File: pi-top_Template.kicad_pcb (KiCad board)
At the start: 2 copper layers, 65 x 56 mm, 6 parts, among them J1 CONN_02X17, J2 CONN_02X17

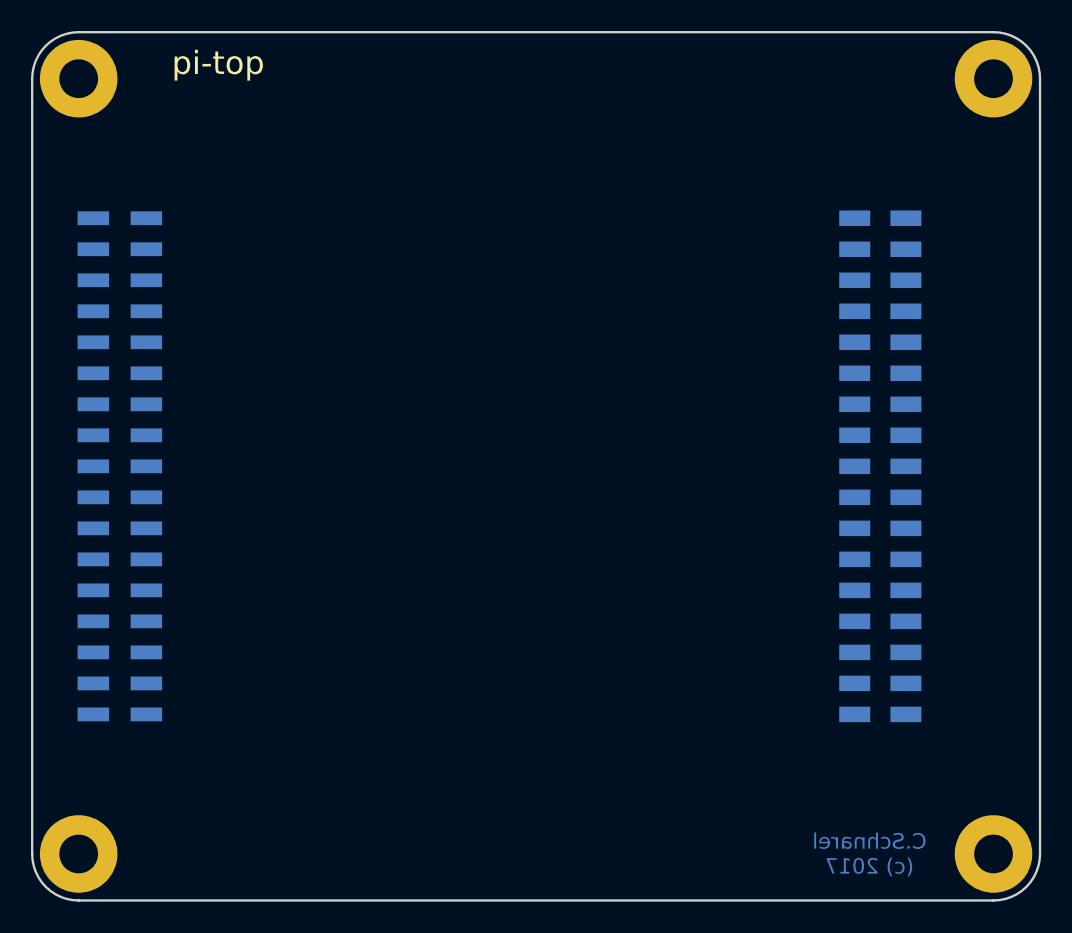
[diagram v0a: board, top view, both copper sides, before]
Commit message: Added board dimentsions
Corrected mounting hole spacing
Corrected connector labeling
Updated README with board size tips
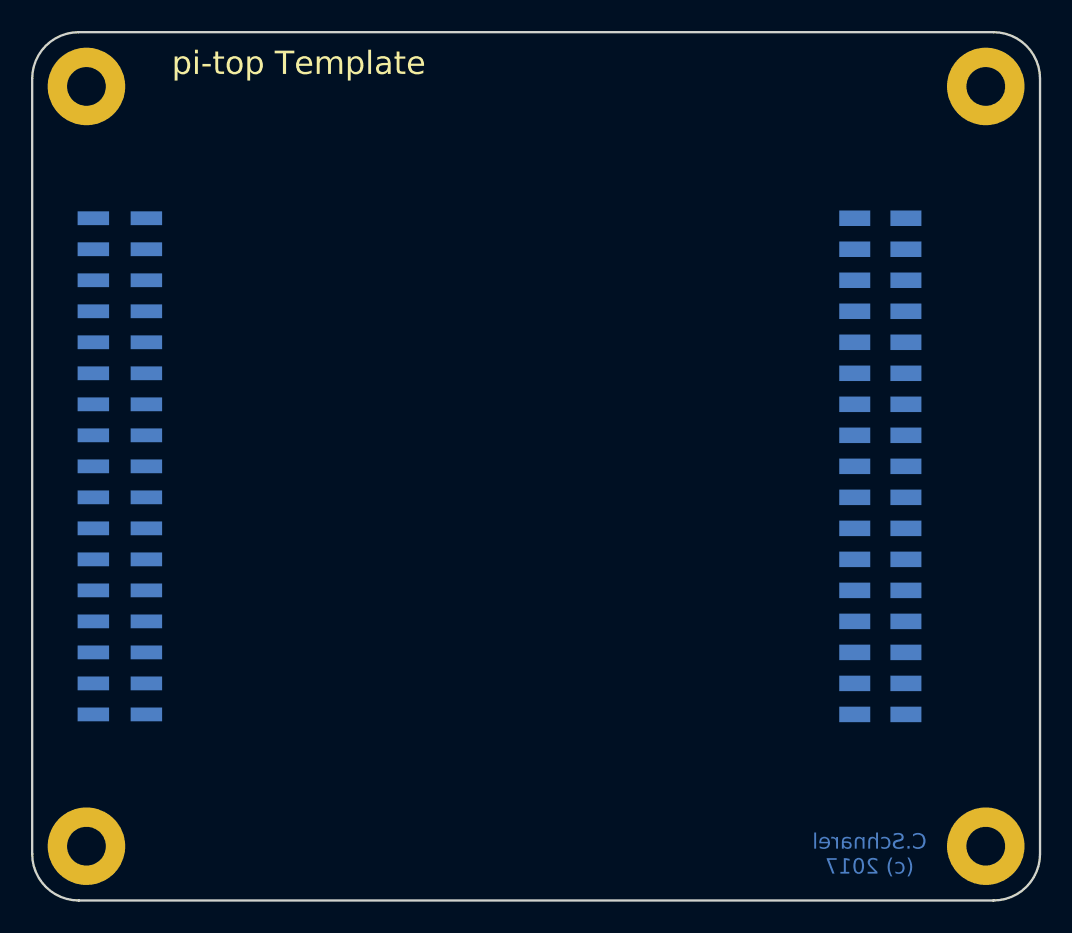
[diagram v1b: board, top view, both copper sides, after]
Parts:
- J1: value CONN_02X17 -> 3M 951 series
- J2: value CONN_02X17 -> Harwin M22-655R
- moved M** 0.71 mm to (41.5, 77.5)
- moved M** 0.71 mm to (99.5, 77.5)
- moved M** 0.71 mm to (99.5, 126.5)
- moved M** 0.71 mm to (41.5, 126.5)
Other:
- board text added: "1"
- board text added: "2"
- board text added: "33"
- board text added: "34"
- board text added: "pi-top Template"
- board text removed: "pi-top"
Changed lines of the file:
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@@
     (links 34)
     (no_connects 34)
-    (area 31.010715 72.5425 109.989286 131.5925)
+    (area 30.067857 66.300001 119.49643 136.700001)
     (thickness 1.6)
-    (drawings 10)
+    (drawings 21)
     (tracks 0)
     (zones 0)
@@
     (zone_45_only no)
     (trace_min 0.2)
-    (segment_width 0.2)
+    (segment_width 0.15)
     (edge_width 0.15)
     (via_size 0.8)
@@
     (pad_to_mask_clearance 0.2)
     (aux_axis_origin 0 0)
-    (visible_elements 7FFFFF7F)
+    (visible_elements 7FFFF77F)
     (pcbplotparams
       (layerselection 0x00030_ffffffff)
@@
     (add_net TXD_BCM-15)
   )
-  (module library:Harwin_M22-5431705 (layer B.Cu)
+  (module library:Harwin_M22-5431705 locked (layer B.Cu)
     (at 43.655 102 270)
     (fp_text reference J1 (at 0 -5 270) (layer B.SilkS)
       (effects (font (size 1 1) (thickness 0.15)) (justify mirror))
     )
-    (fp_text value CONN_02X17 (at 11 -5 270) (layer B.Fab)
+    (fp_text value "3M 951 series" (at 11 -5 270) (layer B.Fab)
       (effects (font (size 1 1) (thickness 0.15)) (justify mirror))
     )
@@
       (net 34 MOSI_BCM-20))
   )
-  (module Mounting_Holes:MountingHole_2.5mm_Pad (layer F.Cu)
-    (at 41 77)
+  (module Mounting_Holes:MountingHole_2.5mm_Pad locked (layer F.Cu)
+    (at 41.5 77.5)
     (descr "Mounting Hole 2.5mm")
     (tags "mounting hole 2.5mm")
@@
     (pad 1 thru_hole circle (at 0 0) (size 5 5) (drill 2.5) (layers *.Cu *.Mask))
   )
-  (module Mounting_Holes:MountingHole_2.5mm_Pad (layer F.Cu)
-    (at 100 77)
+  (module Mounting_Holes:MountingHole_2.5mm_Pad locked (layer F.Cu)
+    (at 99.5 77.5)
     (descr "Mounting Hole 2.5mm")
     (tags "mounting hole 2.5mm")
@@
     (pad 2 thru_hole circle (at 0 0) (size 5 5) (drill 2.5) (layers *.Cu *.Mask))
   )
-  (module Mounting_Holes:MountingHole_2.5mm_Pad (layer F.Cu)
-    (at 100 127)
+  (module Mounting_Holes:MountingHole_2.5mm_Pad locked (layer F.Cu)
+    (at 99.5 126.5)
     (descr "Mounting Hole 2.5mm")
     (tags "mounting hole 2.5mm")
@@
     (pad 3 thru_hole circle (at 0 0) (size 5 5) (drill 2.5) (layers *.Cu *.Mask))
   )
-  (module Mounting_Holes:MountingHole_2.5mm_Pad (layer F.Cu)
-    (at 41 127)
+  (module Mounting_Holes:MountingHole_2.5mm_Pad locked (layer F.Cu)
+    (at 41.5 126.5)
     (descr "Mounting Hole 2.5mm")
     (tags "mounting hole 2.5mm")
@@
     (pad 4 thru_hole circle (at 0 0) (size 5 5) (drill 2.5) (layers *.Cu *.Mask))
   )
-  (module library:Harwin_M22-6553442R (layer B.Cu)
+  (module library:Harwin_M22-6553442R locked (layer B.Cu)
     (at 92.7 102 90)
     (fp_text reference J2 (at 0 -4 90) (layer B.SilkS)
       (effects (font (size 1 1) (thickness 0.15)) (justify mirror))
     )
-    (fp_text value CONN_02X17 (at 12 -4 90) (layer B.Fab)
+    (fp_text value "Harwin M22-655R" (at 12 -4 90) (layer B.Fab)
       (effects (font (size 1 1) (thickness 0.15)) (justify mirror))
     )
@@
       (net 13 HUB_5V))
   )
+  (gr_line (start 87 77.5) (end 96 77.5) (angle 90) (layer Dwgs.User) (width 0.15))
+  (dimension 24.5 (width 0.15) (layer Dwgs.User)
+    (gr_text "24.5 mm" (at 83.15 89.75 270) (layer Dwgs.User)
+      (effects (font (size 1.5 1.5) (thickness 0.15)))
+    )
+    (feature1 (pts (xy 87 102) (xy 81.8 102)))
+    (feature2 (pts (xy 87 77.5) (xy 81.8 77.5)))
+    (crossbar (pts (xy 84.5 77.5) (xy 84.5 102)))
+    (arrow1a (pts (xy 84.5 102) (xy 83.913579 100.873496)))
+    (arrow1b (pts (xy 84.5 102) (xy 85.086421 100.873496)))
+    (arrow2a (pts (xy 84.5 77.5) (xy 83.913579 78.626504)))
+    (arrow2b (pts (xy 84.5 77.5) (xy 85.086421 78.626504)))
+  )
+  (dimension 3.5 (width 0.15) (layer Dwgs.User)
+    (gr_text "3.5 mm" (at 34.5 135 270) (layer Dwgs.User)
+      (effects (font (size 1.5 1.5) (thickness 0.15)))
+    )
+    (feature1 (pts (xy 37 130) (xy 31.8 130)))
+    (feature2 (pts (xy 37 126.5) (xy 31.8 126.5)))
+    (crossbar (pts (xy 34.5 126.5) (xy 34.5 130)))
+    (arrow1a (pts (xy 34.5 130) (xy 33.913579 128.873496)))
+    (arrow1b (pts (xy 34.5 130) (xy 35.086421 128.873496)))
+    (arrow2a (pts (xy 34.5 126.5) (xy 33.913579 127.626504)))
+    (arrow2b (pts (xy 34.5 126.5) (xy 35.086421 127.626504)))
+  )
+  (dimension 49 (width 0.15) (layer Dwgs.User)
+    (gr_text "49.0 mm" (at 110.35 102 270) (layer Dwgs.User)
+      (effects (font (size 1.5 1.5) (thickness 0.15)))
+    )
+    (feature1 (pts (xy 104 126.5) (xy 111.7 126.5)))
+    (feature2 (pts (xy 104 77.5) (xy 111.7 77.5)))
+    (crossbar (pts (xy 109 77.5) (xy 109 126.5)))
+    (arrow1a (pts (xy 109 126.5) (xy 108.413579 125.373496)))
+    (arrow1b (pts (xy 109 126.5) (xy 109.586421 125.373496)))
+    (arrow2a (pts (xy 109 77.5) (xy 108.413579 78.626504)))
+    (arrow2b (pts (xy 109 77.5) (xy 109.586421 78.626504)))
+  )
+  (dimension 3.5 (width 0.15) (layer Dwgs.User)
+    (gr_text "3.5 mm" (at 46.5 134) (layer Dwgs.User)
+      (effects (font (size 1.5 1.5) (thickness 0.15)))
+    )
+    (feature1 (pts (xy 41.5 131) (xy 41.5 136.7)))
+    (feature2 (pts (xy 38 131) (xy 38 136.7)))
+    (crossbar (pts (xy 38 134) (xy 41.5 134)))
+    (arrow1a (pts (xy 41.5 134) (xy 40.373496 134.586421)))
+    (arrow1b (pts (xy 41.5 134) (xy 40.373496 133.413579)))
+    (arrow2a (pts (xy 38 134) (xy 39.126504 134.586421)))
+    (arrow2b (pts (xy 38 134) (xy 39.126504 133.413579)))
+  )
+  (gr_text 33 (at 91 120) (layer B.Mask)
+    (effects (font (size 1 1) (thickness 0.15)) (justify mirror))
+  )
+  (gr_text 34 (at 94.5 120) (layer B.Mask)
+    (effects (font (size 1 1) (thickness 0.15)) (justify mirror))
+  )
+  (gr_text 2 (at 94.5 84) (layer B.Mask)
+    (effects (font (size 1 1) (thickness 0.15)) (justify mirror))
+  )
+  (gr_text 1 (at 91 84) (layer B.Mask)
+    (effects (font (size 1 1) (thickness 0.15)) (justify mirror))
+  )
+  (dimension 56 (width 0.15) (layer Dwgs.User)
+    (gr_text "56.0 mm" (at 114.35 102 270) (layer Dwgs.User)
+      (effects (font (size 1.5 1.5) (thickness 0.15)))
+    )
+    (feature1 (pts (xy 104 130) (xy 115.7 130)))
+    (feature2 (pts (xy 104 74) (xy 115.7 74)))
+    (crossbar (pts (xy 113 74) (xy 113 130)))
+    (arrow1a (pts (xy 113 130) (xy 112.413579 128.873496)))
+    (arrow1b (pts (xy 113 130) (xy 113.586421 128.873496)))
+    (arrow2a (pts (xy 113 74) (xy 112.413579 75.126504)))
+    (arrow2b (pts (xy 113 74) (xy 113.586421 75.126504)))
+  )
+  (dimension 65 (width 0.15) (layer Dwgs.User)
+    (gr_text "65.000 mm" (at 70.5 67.650001) (layer Dwgs.User)
+      (effects (font (size 1.5 1.5) (thickness 0.15)))
+    )
+    (feature1 (pts (xy 38 73) (xy 38 66.300001)))
+    (feature2 (pts (xy 103 73) (xy 103 66.300001)))
+    (crossbar (pts (xy 103 69.000001) (xy 38 69.000001)))
+    (arrow1a (pts (xy 38 69.000001) (xy 39.126504 68.41358)))
+    (arrow1b (pts (xy 38 69.000001) (xy 39.126504 69.586422)))
+    (arrow2a (pts (xy 103 69.000001) (xy 101.873496 68.41358)))
+    (arrow2b (pts (xy 103 69.000001) (xy 101.873496 69.586422)))
+  )
   (gr_text "C.Schnarel\n(c) 2017" (at 92 127) (layer B.Cu)
     (effects (font (size 1 1) (thickness 0.15)) (justify mirror))
   )
-  (gr_text pi-top (at 47 76) (layer F.SilkS)
+  (gr_text "pi-top Template" (at 47 76) (layer F.SilkS)
     (effects (font (size 1.5 1.5) (thickness 0.3)) (justify left))
   )

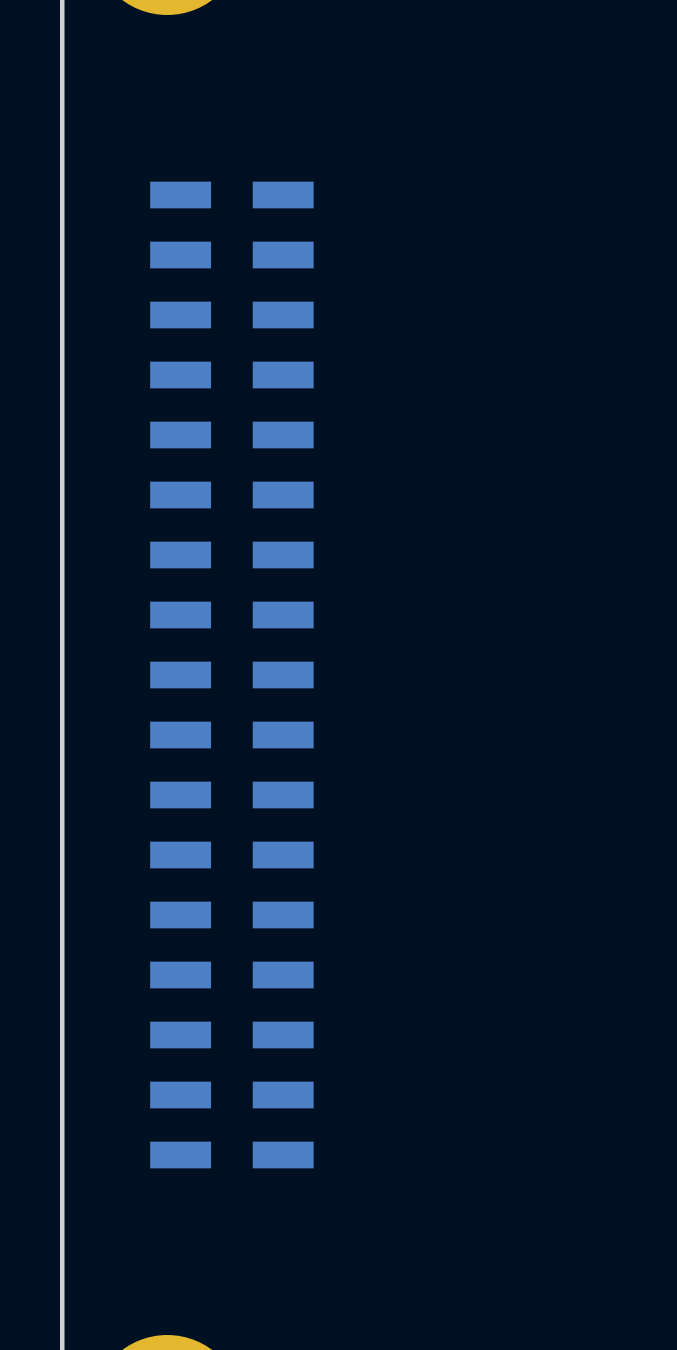
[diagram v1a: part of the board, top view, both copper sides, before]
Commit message: Saving footprints with project
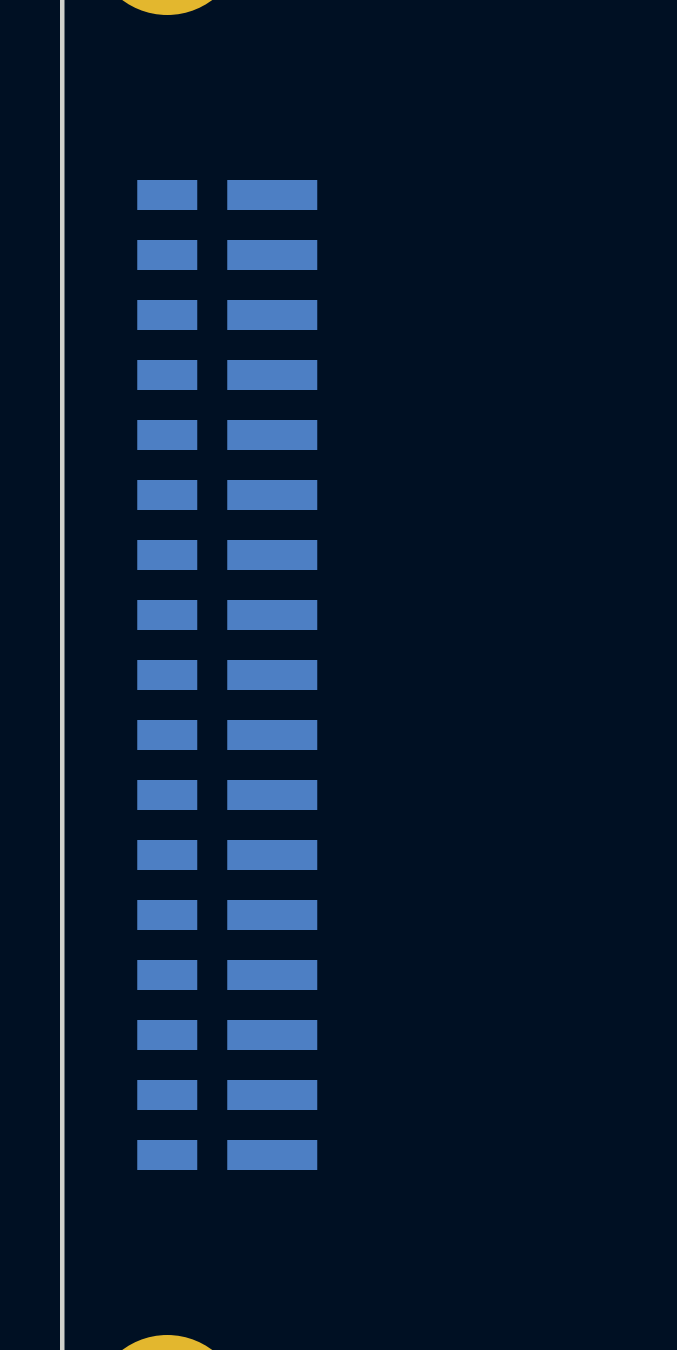
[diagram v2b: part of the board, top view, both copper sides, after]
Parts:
- J1: footprint library:Harwin_M22-5431705 -> library:3M_951217-4620-XX
- moved J1 1.20 mm to (43.0, 101.0)

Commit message: Shuffling files around for a "standard" workspace
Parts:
- J1: value 3M 951 series -> 3M 951 Series
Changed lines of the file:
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@@
 (kicad_pcb (version 20170123) (host pcbnew "(2017-05-14 revision 14bb238b3)-makepkg")
   (general
-    (links 0)
+    (links 34)
     (no_connects 34)
     (area 30.067857 66.300001 119.49643 136.700001)
     (thickness 1.6)
-    (drawings 21)
+    (drawings 25)
     (tracks 0)
     (zones 0)
@@
       (effects (font (size 1 1) (thickness 0.15)) (justify mirror))
     )
-    (fp_text value "3M 951 series" (at 12 -5 270) (layer B.Fab)
+    (fp_text value "3M 951 Series" (at 12 -5 270) (layer B.Fab)
       (effects (font (size 1 1) (thickness 0.15)) (justify mirror))
     )
@@
       (net 13 HUB_5V))
   )
+  (gr_text 34 (at 41.5 120) (layer B.SilkS)
+    (effects (font (size 1 1) (thickness 0.15)) (justify mirror))
+  )
+  (gr_text 33 (at 45 120) (layer B.SilkS)
+    (effects (font (size 1 1) (thickness 0.15)) (justify mirror))
+  )
+  (gr_text 1 (at 45 84) (layer B.SilkS)
+    (effects (font (size 1 1) (thickness 0.15)) (justify mirror))
+  )
+  (gr_text 2 (at 41.5 84) (layer B.SilkS)
+    (effects (font (size 1 1) (thickness 0.15)) (justify mirror))
+  )
   (gr_line (start 87 77.5) (end 96 77.5) (angle 90) (layer Dwgs.User) (width 0.15))
   (dimension 24.5 (width 0.15) (layer Dwgs.User)
@@
     (arrow2b (pts (xy 38 134) (xy 39.126504 133.413579)))
   )
-  (gr_text 33 (at 91 120) (layer B.Mask)
-    (effects (font (size 1 1) (thickness 0.15)) (justify mirror))
-  )
-  (gr_text 34 (at 94.5 120) (layer B.Mask)
-    (effects (font (size 1 1) (thickness 0.15)) (justify mirror))
-  )
-  (gr_text 2 (at 94.5 84) (layer B.Mask)
-    (effects (font (size 1 1) (thickness 0.15)) (justify mirror))
-  )
-  (gr_text 1 (at 91 84) (layer B.Mask)
-    (effects (font (size 1 1) (thickness 0.15)) (justify mirror))
-  )
+  (gr_text 33 (at 91 120) (layer B.SilkS)
+    (effects (font (size 1 1) (thickness 0.15)) (justify mirror))
+  )
+  (gr_text 34 (at 94.5 120) (layer B.SilkS)
+    (effects (font (size 1 1) (thickness 0.15)) (justify mirror))
+  )
+  (gr_text 2 (at 94.5 84) (layer B.SilkS)
+    (effects (font (size 1 1) (thickness 0.15)) (justify mirror))
+  )
+  (gr_text 1 (at 91 84) (layer B.SilkS)
+    (effects (font (size 1 1) (thickness 0.15)) (justify mirror))
+  )
